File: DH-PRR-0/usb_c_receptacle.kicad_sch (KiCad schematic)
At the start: 3 parts, among them J1 USB_C_Receptacle_USB2.0_16P

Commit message: alternate power topologies
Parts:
- renumbered R11 to R28, R12 to R29
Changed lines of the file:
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@@
 		(dnp no)
 		(fields_autoplaced yes)
-		(property "Reference" "#PWR026"
+		(property "Reference" "#PWR053"
 			(at 191.77 158.75 0)
 			(hide yes)
@@
 			(project "DH-PRR-0"
 				(path "/ef4cbb1a-0736-46e9-bda5-652f30ffa2fe/e3608c0e-4ba9-4be0-a463-77fe1c953085"
-					(reference "#PWR026")
+					(reference "#PWR053")
 					(unit 1)
 				)
@@
 		(dnp no)
 		(fields_autoplaced yes)
-		(property "Reference" "#PWR028"
+		(property "Reference" "#PWR055"
 			(at 215.9 127 0)
 			(hide yes)
@@
 			(project "DH-PRR-0"
 				(path "/ef4cbb1a-0736-46e9-bda5-652f30ffa2fe/e3608c0e-4ba9-4be0-a463-77fe1c953085"
-					(reference "#PWR028")
+					(reference "#PWR055")
 					(unit 1)
 				)
@@
 		(in_pos_files yes)
 		(dnp no)
-		(property "Reference" "R12"
+		(property "Reference" "R29"
 			(at 210.82 121.92 90)
 			(show_name no)
@@
 			(project "DH-PRR-0"
 				(path "/ef4cbb1a-0736-46e9-bda5-652f30ffa2fe/e3608c0e-4ba9-4be0-a463-77fe1c953085"
-					(reference "R12")
+					(reference "R29")
 					(unit 1)
 				)
@@
 		(in_pos_files yes)
 		(dnp no)
-		(property "Reference" "R11"
+		(property "Reference" "R28"
 			(at 210.82 114.3 90)
 			(show_name no)
@@
 			(project "DH-PRR-0"
 				(path "/ef4cbb1a-0736-46e9-bda5-652f30ffa2fe/e3608c0e-4ba9-4be0-a463-77fe1c953085"
-					(reference "R11")
+					(reference "R28")
 					(unit 1)
 				)
@@
 		(dnp no)
 		(fields_autoplaced yes)
-		(property "Reference" "#PWR027"
+		(property "Reference" "#PWR054"
 			(at 208.28 114.3 0)
 			(hide yes)
@@
 			(project "DH-PRR-0"
 				(path "/ef4cbb1a-0736-46e9-bda5-652f30ffa2fe/e3608c0e-4ba9-4be0-a463-77fe1c953085"
-					(reference "#PWR027")
-					(unit 1)
-				)
+					(reference "#PWR054")
+					(unit 1)
+				)

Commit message: mcu bootmode
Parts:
- renumbered R28 to R11, R29 to R12
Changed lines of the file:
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@@
 		(dnp no)
 		(fields_autoplaced yes)
-		(property "Reference" "#PWR053"
+		(property "Reference" "#PWR039"
 			(at 191.77 158.75 0)
 			(hide yes)
@@
 			(project "DH-PRR-0"
 				(path "/ef4cbb1a-0736-46e9-bda5-652f30ffa2fe/e3608c0e-4ba9-4be0-a463-77fe1c953085"
-					(reference "#PWR053")
+					(reference "#PWR039")
 					(unit 1)
 				)
@@
 		(dnp no)
 		(fields_autoplaced yes)
-		(property "Reference" "#PWR055"
+		(property "Reference" "#PWR041"
 			(at 215.9 127 0)
 			(hide yes)
@@
 			(project "DH-PRR-0"
 				(path "/ef4cbb1a-0736-46e9-bda5-652f30ffa2fe/e3608c0e-4ba9-4be0-a463-77fe1c953085"
-					(reference "#PWR055")
+					(reference "#PWR041")
 					(unit 1)
 				)
@@
 		(in_pos_files yes)
 		(dnp no)
-		(property "Reference" "R29"
+		(property "Reference" "R12"
 			(at 210.82 121.92 90)
 			(show_name no)
@@
 			(project "DH-PRR-0"
 				(path "/ef4cbb1a-0736-46e9-bda5-652f30ffa2fe/e3608c0e-4ba9-4be0-a463-77fe1c953085"
-					(reference "R29")
+					(reference "R12")
 					(unit 1)
 				)
@@
 		(in_pos_files yes)
 		(dnp no)
-		(property "Reference" "R28"
+		(property "Reference" "R11"
 			(at 210.82 114.3 90)
 			(show_name no)
@@
 			(project "DH-PRR-0"
 				(path "/ef4cbb1a-0736-46e9-bda5-652f30ffa2fe/e3608c0e-4ba9-4be0-a463-77fe1c953085"
-					(reference "R28")
+					(reference "R11")
 					(unit 1)
 				)
@@
 		(dnp no)
 		(fields_autoplaced yes)
-		(property "Reference" "#PWR054"
+		(property "Reference" "#PWR040"
 			(at 208.28 114.3 0)
 			(hide yes)
@@
 			(project "DH-PRR-0"
 				(path "/ef4cbb1a-0736-46e9-bda5-652f30ffa2fe/e3608c0e-4ba9-4be0-a463-77fe1c953085"
-					(reference "#PWR054")
-					(unit 1)
-				)
+					(reference "#PWR040")
+					(unit 1)
+				)

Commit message: i dont remember
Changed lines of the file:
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@@
 	(wire
 		(pts
-			(xy 208.28 110.49) (xy 208.28 111.76)
+			(xy 208.28 109.22) (xy 208.28 111.76)
 		)
 		(stroke
@@
 	(symbol
 		(lib_id "power:VBUS")
-		(at 208.28 110.49 0)
+		(at 208.28 109.22 0)
 		(unit 1)
 		(body_style 1)
@@
 		(fields_autoplaced yes)
 		(property "Reference" "#PWR040"
-			(at 208.28 114.3 0)
+			(at 208.28 113.03 0)
 			(hide yes)
 			(show_name no)
@@
 		)
 		(property "Value" "VBUS"
-			(at 208.28 105.41 0)
+			(at 208.28 104.14 0)
 			(show_name no)
 			(do_not_autoplace no)
@@
 		)
 		(property "Footprint" ""
-			(at 208.28 110.49 0)
+			(at 208.28 109.22 0)
 			(hide yes)
 			(show_name no)
@@
 		)
 		(property "Datasheet" ""
-			(at 208.28 110.49 0)
+			(at 208.28 109.22 0)
 			(hide yes)
 			(show_name no)
@@
 		)
 		(property "Description" "Power symbol creates a global label with name \"VBUS\""
-			(at 208.28 110.49 0)
-			(hide yes)
-			(show_name no)
+			(at 208.28 109.22 0)
+			(hide yes)
+			(show_name no)

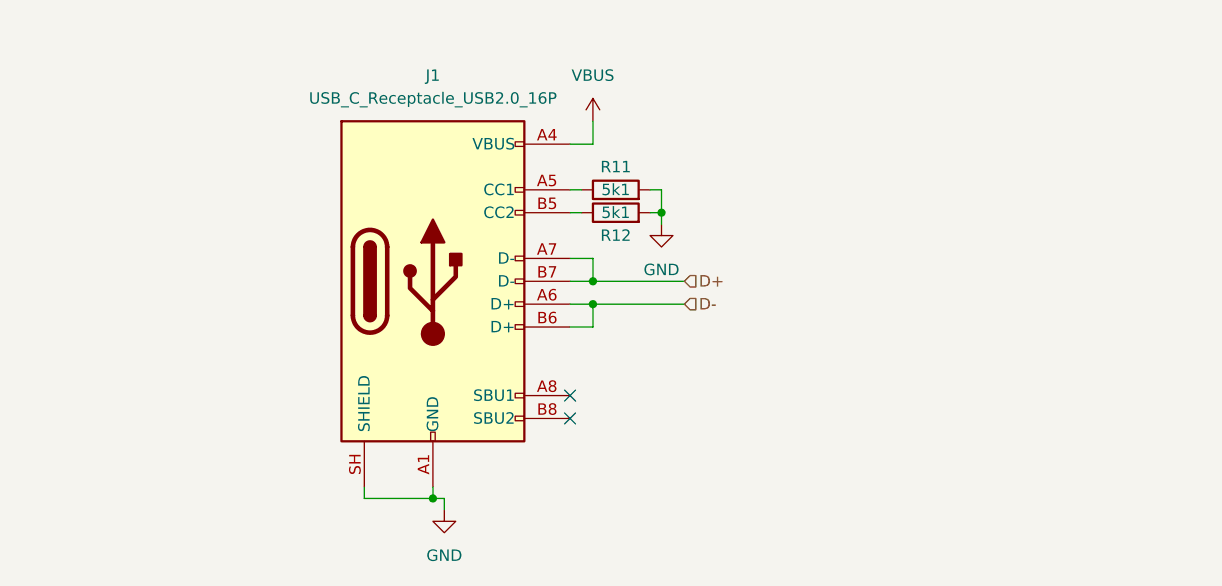
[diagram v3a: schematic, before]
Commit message: uart IC to use USB interface for memory instead
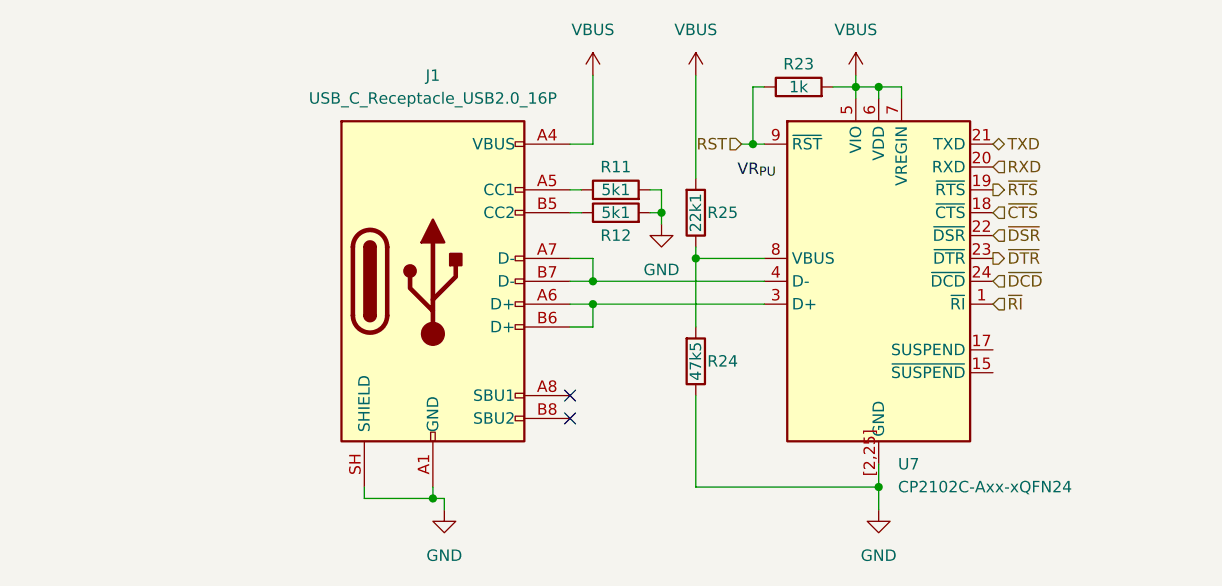
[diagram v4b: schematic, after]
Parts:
- added R23: 1k, Package_DFN_QFN:WQFN-24-1EP_4x4mm_P0.5mm_EP2.45x2.45mm, symbol Device:R
- added R24: 47k5, symbol Device:R
- added R25: 22k1, symbol Device:R
- added U7: CP2102C-Axx-xQFN24, Package_DFN_QFN:WQFN-24-1EP_4x4mm_P0.5mm_EP2.45x2.45mm, symbol Interface_USB:CP2102C-Axx-xQFN24
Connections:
- net GND: now also R24.1, U7.[2,25] (GND)
- net VBUS: now also R23.2, R25.2, U7.5 (VIO), U7.6 (VDD), U7.7 (VREGIN)
- net D+: no longer names the net of J1.A7 (D-), J1.B7 (D-)
- net D+: now also U7.4 (D-)
- net D-: no longer names the net of J1.A6 (D+), J1.B6 (D+)
- net D-: now also U7.3 (D+)
- new net: R24.2, R25.1, U7.8 (VBUS)
- new net RST: R23.1, U7.9 (~{RST})
- new net RXD: U7.20 (RXD)
- new net TXD: U7.21 (TXD)
- new net ~{CTS}: U7.18 (~{CTS})
- new net ~{DCD}: U7.24 (~{DCD})
- new net ~{DSR}: U7.22 (~{DSR})
- new net ~{DTR}: U7.23 (~{DTR})
- new net ~{RI}: U7.1 (~{RI})
- new net ~{RTS}: U7.19 (~{RTS})

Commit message: reorganized antennas
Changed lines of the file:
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@@
 	(wire
 		(pts
-			(xy 215.9 120.65) (xy 215.9 119.38)
+			(xy 215.9 152.4) (xy 215.9 119.38)
 		)
 		(stroke
 			(width 0)
 			(type default)
-		)
-	)
-	(label "VR_{PU}"
-		(at 228.6 115.57 180)
-		(effects
-			(font
-				(size 1.27 1.27)
-			)
-			(justify right bottom)
 		)
 	)
@@
 	(symbol
 		(lib_id "power:GND")
-		(at 215.9 120.65 0)
+		(at 215.9 152.4 0)
 		(unit 1)
 		(body_style 1)
@@
 		(fields_autoplaced yes)
 		(property "Reference" "#PWR041"
-			(at 215.9 127 0)
+			(at 215.9 158.75 0)
 			(hide yes)
 			(show_name no)
@@
 		)
 		(property "Value" "GND"
-			(at 215.9 125.73 0)
+			(at 215.9 157.48 0)
 			(show_name no)
 			(do_not_autoplace no)
@@
 		)
 		(property "Footprint" ""
-			(at 215.9 120.65 0)
+			(at 215.9 152.4 0)
 			(hide yes)
 			(show_name no)
@@
 		)
 		(property "Datasheet" ""
-			(at 215.9 120.65 0)
+			(at 215.9 152.4 0)
 			(hide yes)
 			(show_name no)
@@
 		)
 		(property "Description" "Power symbol creates a global label with name \"GND\" , ground"
-			(at 215.9 120.65 0)
-			(hide yes)
-			(show_name no)
+			(at 215.9 152.4 0)
+			(hide yes)
+			(show_name no)

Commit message: added usb to spi to free up USB bus
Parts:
- added C20: u1, symbol Device:C
- added C21: 1u, symbol Device:C
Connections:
- net GND: now also C20.2, C21.2
- net VBUS: no longer R23.2, U7.5 (VIO), U7.6 (VDD), U7.7 (VREGIN)
- net ~{SUSPEND}: now reaches U7.15 (~{SUSPEND})
- net SUSPEND: now reaches U7.17 (SUSPEND)
- net ~{CTS}: no longer names the net of U7.18 (~{CTS})
- net ~{DCD}: no longer names the net of U7.24 (~{DCD})
- net ~{DSR}: no longer names the net of U7.22 (~{DSR})
- net ~{RTS}: no longer names the net of U7.19 (~{RTS})
- new net +3V3: C20.1, R23.2, U7.5 (VIO), U7.6 (VDD)
- new net +5V: C21.1, U7.7 (VREGIN)
- no-connect marks 2 -> 6
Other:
- moved on the sheet: J1, R11, R12, R23, R24, R25, U7

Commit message: changed usb-spi bridge to host bridge, now functional
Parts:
- renumbered R11 to R16, R12 to R17, R25 to R18, R24 to R19, R23 to R20
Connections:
- net ~{DTR}: no longer names the net of U7.23 (~{DTR})
- net ~{RI}: no longer names the net of U7.1 (~{RI})
- no-connect marks 6 -> 8
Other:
- moved on the sheet: C20, C21
